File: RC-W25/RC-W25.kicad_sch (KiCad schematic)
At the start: 0 parts

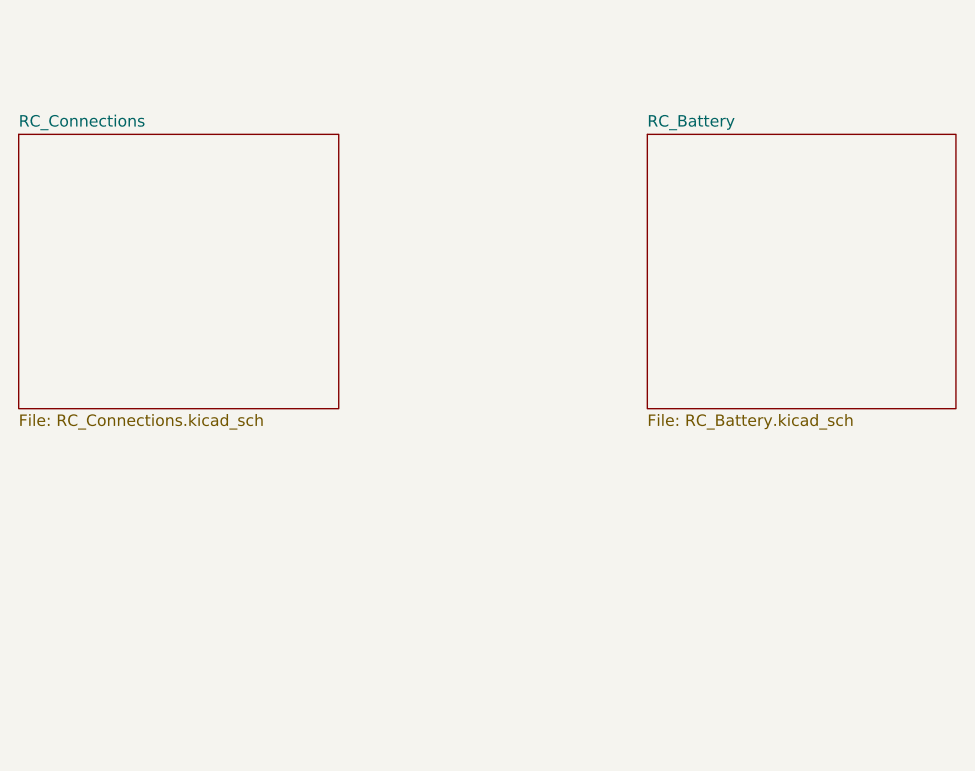
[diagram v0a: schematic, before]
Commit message: Schematic Update
Added buttons with debouncing and DC motor duraclik connector
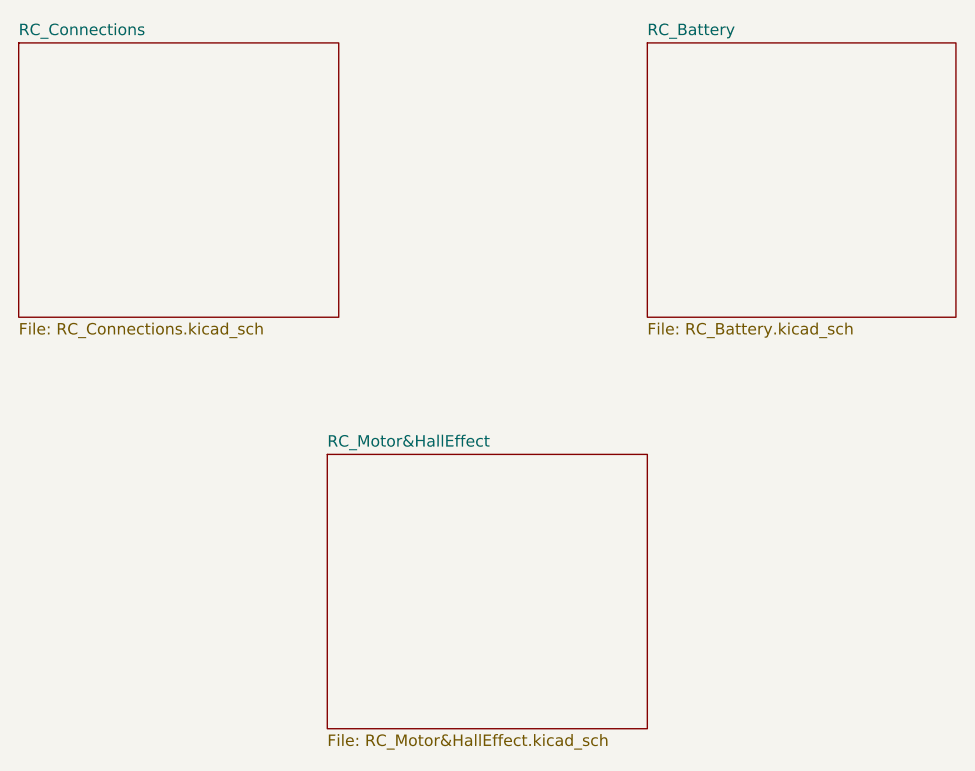
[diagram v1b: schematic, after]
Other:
- added sheet RC_Motor&HallEffect (RC_Motor&HallEffect.kicad_sch)
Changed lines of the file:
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@@
 	(paper "A4")
 	(sheet
-		(at 90.17 72.39)
+		(at 90.17 62.23)
 		(size 35.56 30.48)
 		(fields_autoplaced yes)
@@
 		)
 		(property "Sheetname" "RC_Connections"
-			(at 90.17 71.6784 0)
+			(at 90.17 61.5184 0)
 			(effects
 				(font
@@
 		)
 		(property "Sheetfile" "RC_Connections.kicad_sch"
-			(at 90.17 103.4546 0)
+			(at 90.17 93.2946 0)
 			(effects
 				(font
@@
 	)
 	(sheet
-		(at 160.02 72.39)
+		(at 124.46 107.95)
+		(size 35.56 30.48)
+		(fields_autoplaced yes)
+		(stroke
+			(width 0.1524)
+			(type solid)
+		)
+		(fill
+			(color 255 255 194 1.0000)
+		)
+		(property "Sheetname" "RC_Motor&HallEffect"
+			(at 124.46 107.2384 0)
+			(effects
+				(font
+					(size 1.27 1.27)
+				)
+				(justify left bottom)
+			)
+		)
+		(property "Sheetfile" "RC_Motor&HallEffect.kicad_sch"
+			(at 124.46 139.0146 0)
+			(effects
+				(font
+					(size 1.27 1.27)
+				)
+				(justify left top)
+			)
+		)
+		(instances
+			(project "RC-W25"
+				(path "/427b2895-e3a6-4096-b101-5f65a3f7473e"
+					(page "4")
+				)
+			)
+		)
+	)
+	(sheet
+		(at 160.02 62.23)
 		(size 34.29 30.48)
 		(fields_autoplaced yes)
@@
 		)
 		(property "Sheetname" "RC_Battery"
-			(at 160.02 71.6784 0)
+			(at 160.02 61.5184 0)
 			(effects
 				(font
@@
 		)
 		(property "Sheetfile" "RC_Battery.kicad_sch"
-			(at 160.02 103.4546 0)
+			(at 160.02 93.2946 0)
 			(effects
 				(font
